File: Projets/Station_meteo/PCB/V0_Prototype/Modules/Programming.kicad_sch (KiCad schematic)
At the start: 14 parts, among them J28 SolderJumper_2_Bridged, J29 USB_C_Receptacle_USB2.0_16P, J34 SolderJumper_2_Bridged, U10 USBLC6-2P6, U11 CH340G, U12 AMS1117-3.3, Y3 12MHz

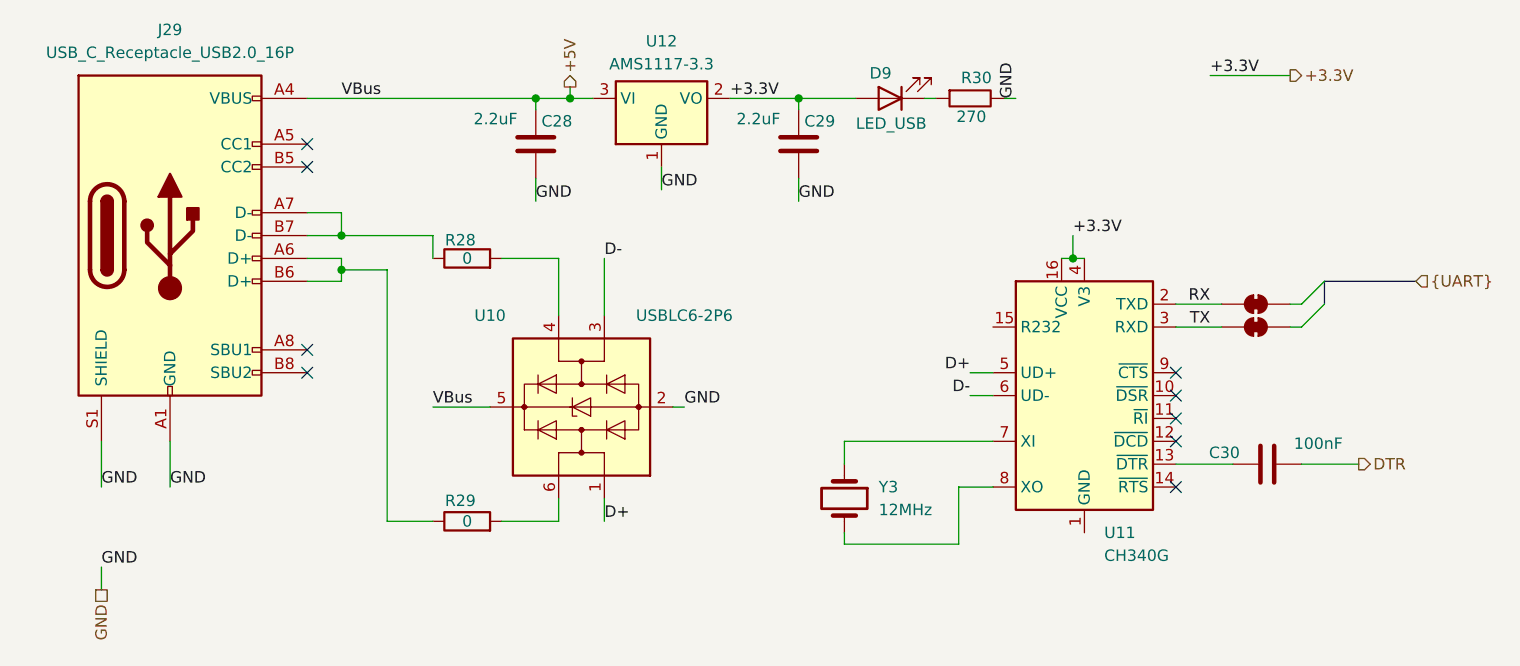
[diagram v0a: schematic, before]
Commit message: Add V1 THT version
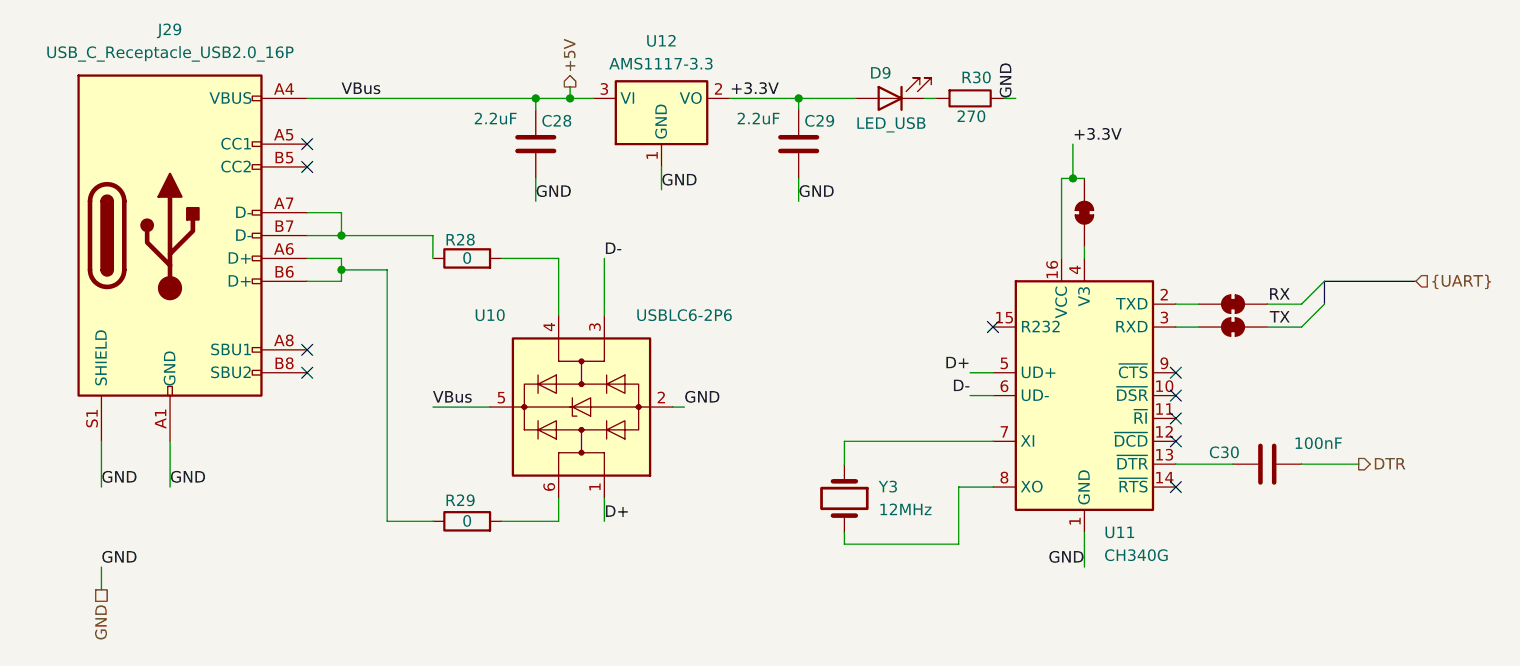
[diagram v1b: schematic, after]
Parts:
- added J40: SolderJumper_2_Bridged, Jumper:SolderJumper-2_P1.3mm_Bridged_Pad1.0x1.5mm, symbol Jumper:SolderJumper_2_Bridged
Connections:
- net +3.3V: now also J40.2 (B); no longer U11.4 (V3)
- net GND: now also U11.1 (GND)
- net RX: now also J28.2 (B); no longer J28.1 (A), U11.2 (TXD)
- net TX: now also J34.2 (B); no longer J34.1 (A), U11.3 (RXD)
- new net: J28.1 (A), U11.2 (TXD)
- new net: J34.1 (A), U11.3 (RXD)
- new net: J40.1 (A), U11.4 (V3)
- no-connect marks 9 -> 10
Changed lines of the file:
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@@
 		(rev "1.0")
+	)
+	(bus_alias "I2C"
+		(members "SCL" "SDA")
+	)
+	(bus_alias "SPI"
+		(members "MOSI" "MISO" "SCK" "CLK")
+	)
+	(bus_alias "UART"
+		(members "RX" "TX")
 	)
 	(junction
@@
 	)
 	(junction
-		(at 133.35 46.99)
+		(at 52.07 44.45)
 		(diameter 0)
 		(color 0 0 0 0)
 	)
 	(junction
-		(at 52.07 44.45)
+		(at 133.35 38.1)
 		(diameter 0)
 		(color 0 0 0 0)
@@
 		(at 48.26 36.83)
 	)
+	(no_connect
+		(at 124.46 54.61)
+	)
 	(bus_entry
 		(at 161.29 52.07)
@@
 	(wire
 		(pts
-			(xy 157.48 54.61) (xy 158.75 54.61)
+			(xy 154.94 54.61) (xy 158.75 54.61)
 		)
 		(stroke
@@
 	(wire
 		(pts
+			(xy 134.62 45.72) (xy 134.62 46.99)
+		)
+		(stroke
+			(width 0)
+			(type default)
+		)
+	)
+	(wire
+		(pts
 			(xy 52.07 44.45) (xy 62.23 44.45)
 		)
@@
 	(wire
 		(pts
-			(xy 132.08 46.99) (xy 133.35 46.99)
-		)
-		(stroke
-			(width 0)
-			(type default)
-		)
-	)
-	(wire
-		(pts
-			(xy 144.78 52.07) (xy 149.86 52.07)
+			(xy 144.78 52.07) (xy 147.32 52.07)
+		)
+		(stroke
+			(width 0)
+			(type default)
+		)
+	)
+	(wire
+		(pts
+			(xy 132.08 38.1) (xy 133.35 38.1)
 		)
 		(stroke
@@
 	(wire
 		(pts
-			(xy 148.59 26.67) (xy 157.48 26.67)
-		)
-		(stroke
-			(width 0)
-			(type default)
-		)
-	)
-	(wire
-		(pts
 			(xy 107.95 78.74) (xy 107.95 77.47)
 		)
@@
 	(wire
 		(pts
+			(xy 134.62 77.47) (xy 134.62 81.28)
+		)
+		(stroke
+			(width 0)
+			(type default)
+		)
+	)
+	(wire
+		(pts
 			(xy 107.95 67.31) (xy 124.46 67.31)
 		)
@@
 	(wire
 		(pts
-			(xy 133.35 46.99) (xy 134.62 46.99)
-		)
-		(stroke
-			(width 0)
-			(type default)
-		)
-	)
-	(wire
-		(pts
 			(xy 73.66 38.1) (xy 73.66 40.64)
 		)
@@
 	(wire
 		(pts
-			(xy 144.78 54.61) (xy 149.86 54.61)
+			(xy 144.78 54.61) (xy 147.32 54.61)
 		)
 		(stroke
@@
 	(wire
 		(pts
-			(xy 157.48 52.07) (xy 158.75 52.07)
+			(xy 154.94 52.07) (xy 158.75 52.07)
+		)
+		(stroke
+			(width 0)
+			(type default)
+		)
+	)
+	(wire
+		(pts
+			(xy 132.08 46.99) (xy 132.08 38.1)
 		)
 		(stroke
@@
 	(wire
 		(pts
-			(xy 133.35 44.45) (xy 133.35 46.99)
+			(xy 133.35 38.1) (xy 134.62 38.1)
+		)
+		(stroke
+			(width 0)
+			(type default)
+		)
+	)
+	(wire
+		(pts
+			(xy 133.35 34.29) (xy 133.35 38.1)
 		)
 		(stroke
@@
 	)
 	(label "RX"
-		(at 148.59 52.07 180)
+		(at 157.48 52.07 180)
 		(fields_autoplaced yes)
 		(effects
@@
 	)
 	(label "+3.3V"
-		(at 133.35 44.45 0)
+		(at 133.35 34.29 0)
 		(fields_autoplaced yes)
 		(effects
@@
 		)
 	)
-	(label "+3.3V"
-		(at 148.59 26.67 0)
-		(fields_autoplaced yes)
-		(effects
-			(font
-				(size 1.27 1.27)
-			)
-			(justify left bottom)
-		)
-	)
 	(label "GND"
 		(at 102.87 40.64 0)
@@
 	)
 	(label "TX"
-		(at 148.59 54.61 180)
+		(at 157.48 54.61 180)
+		(fields_autoplaced yes)
+		(effects
+			(font
+				(size 1.27 1.27)
+			)
+			(justify right bottom)
+		)
+	)
+	(label "GND"
+		(at 134.62 81.28 180)
 		(fields_autoplaced yes)
 		(effects
@@
 		(shape output)
 		(at 77.47 27.94 90)
-		(fields_autoplaced yes)
-		(effects
-			(font
-				(size 1.27 1.27)
-			)
-			(justify left)
-		)
-	)
-	(hierarchical_label "+3.3V"
-		(shape output)
-		(at 157.48 26.67 0)
 		(fields_autoplaced yes)
 		(effects
@@
 	(symbol
 		(lib_id "Jumper:SolderJumper_2_Bridged")
-		(at 153.67 52.07 0)
+		(at 151.13 52.07 0)
 		(unit 1)
 		(exclude_from_sim yes)
@@
 		(fields_autoplaced yes)
 		(property "Reference" "J28"
-			(at 153.67 45.72 0)
+			(at 151.13 45.72 0)
 			(effects
 				(font
@@
 		)
 		(property "Value" "SolderJumper_2_Bridged"
-			(at 153.67 48.26 0)
+			(at 151.13 48.26 0)
 			(effects
 				(font
@@
 		)
 		(property "Footprint" "Jumper:SolderJumper-2_P1.3mm_Bridged_Pad1.0x1.5mm"
-			(at 153.67 52.07 0)
+			(at 151.13 52.07 0)
 			(effects
 				(font
@@
 		)
 		(property "Datasheet" "~"
-			(at 153.67 52.07 0)
+			(at 151.13 52.07 0)
 			(effects
 				(font
@@
 		)
 		(property "Description" "Solder Jumper, 2-pole, closed/bridged"
-			(at 153.67 52.07 0)
+			(at 151.13 52.07 0)
 			(effects
 				(font
@@
 	(symbol
 		(lib_id "Jumper:SolderJumper_2_Bridged")
-		(at 153.67 54.61 0)
+		(at 151.13 54.61 0)
 		(unit 1)
 		(exclude_from_sim yes)
@@
 		(fields_autoplaced yes)
 		(property "Reference" "J34"
-			(at 153.67 48.26 0)
+			(at 151.13 48.26 0)
 			(effects
 				(font
@@
 		)
 		(property "Value" "SolderJumper_2_Bridged"
-			(at 153.67 50.8 0)
+			(at 151.13 50.8 0)
 			(effects
 				(font
@@
 		)
 		(property "Footprint" "Jumper:SolderJumper-2_P1.3mm_Bridged_Pad1.0x1.5mm"
-			(at 153.67 54.61 0)
+			(at 151.13 54.61 0)
 			(effects
 				(font
@@
 		)
 		(property "Datasheet" "~"
-			(at 153.67 54.61 0)
+			(at 151.13 54.61 0)
 			(effects
 				(font
@@
 		)
 		(property "Description" "Solder Jumper, 2-pole, closed/bridged"
-			(at 153.67 54.61 0)
+			(at 151.13 54.61 0)
 			(effects
 				(font
@@
 					(unit 1)
 				)
+			)
+		)
+	)
+	(symbol
+		(lib_id "Jumper:SolderJumper_2_Bridged")
+		(at 134.62 41.91 90)
+		(unit 1)
+		(exclude_from_sim yes)
+		(in_bom no)
+		(on_board yes)
+		(dnp no)
+		(fields_autoplaced yes)
+		(property "Reference" "J40"
+			(at 128.27 41.91 0)
+			(effects
+				(font
+					(size 1.27 1.27)
+				)
+				(hide yes)
+			)
+		)
+		(property "Value" "SolderJumper_2_Bridged"
+			(at 130.81 41.91 0)
+			(effects
+				(font
+					(size 1.27 1.27)
+				)
+				(hide yes)
+			)
+		)
+		(property "Footprint" "Jumper:SolderJumper-2_P1.3mm_Bridged_Pad1.0x1.5mm"
+			(at 134.62 41.91 0)
+			(effects
+				(font
+					(size 1.27 1.27)
+				)
+				(hide yes)
+			)
+		)
+		(property "Datasheet" "~"
+			(at 134.62 41.91 0)
+			(effects
+				(font
+					(size 1.27 1.27)
+				)
+				(hide yes)
+			)
+		)
+		(property "Description" "Solder Jumper, 2-pole, closed/bridged"
+			(at 134.62 41.91 0)
+			(effects
+				(font
+					(size 1.27 1.27)
+				)
+				(hide yes)
+			)
+		)
+		(pin "1"
+		)
+		(pin "2"
+		)
+		(instances
+			(project "Weather"
+				(path "/4bc9f80e-0a24-4618-ba5d-3a118070c43e/f0228972-90ea-4da6-b918-ead9c247762d"
+					(reference "J40")
+					(unit 1)
+				)
